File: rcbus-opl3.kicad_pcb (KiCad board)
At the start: 2 copper layers, 100 x 50 mm, 39 parts, among them CON1 SJ1-3523N, P1 RC2014 BUS, U1 74HCT688, U2 YMF262, U3 YAC512, U4 TL074, Y1 SG-8002CA

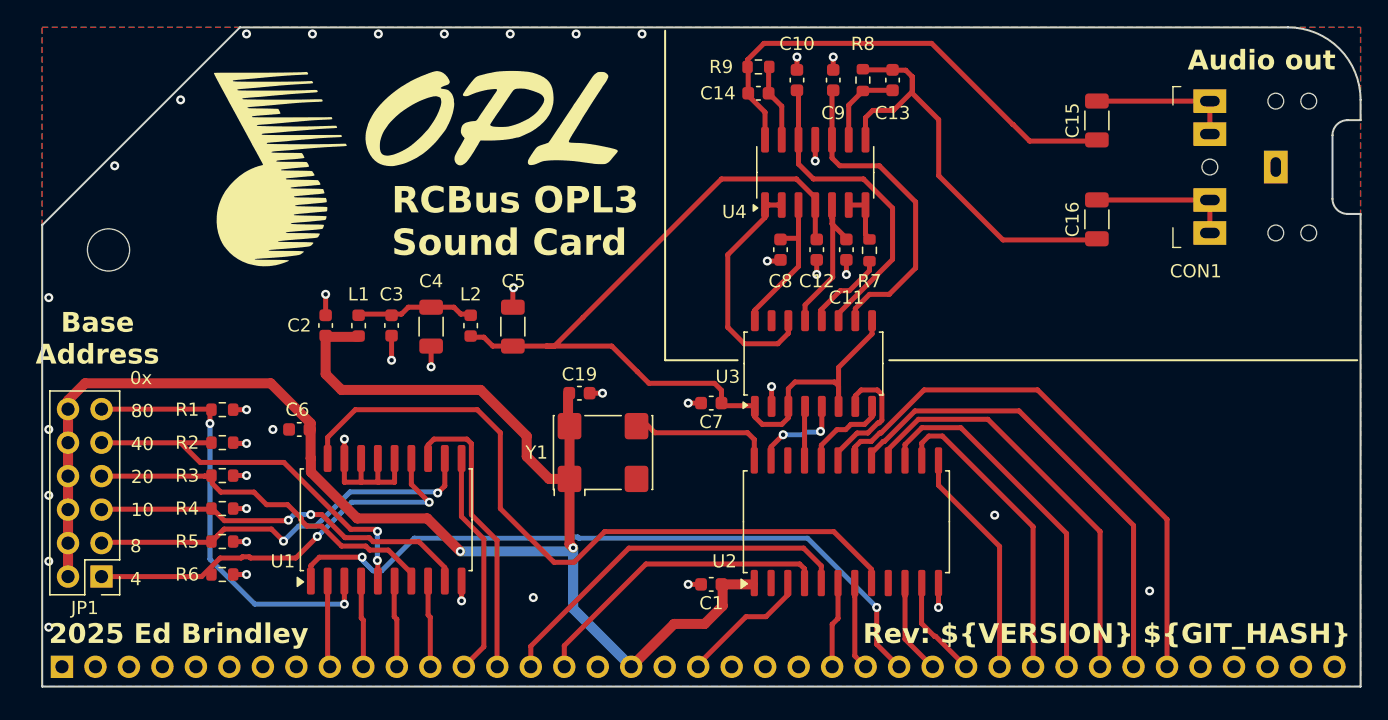
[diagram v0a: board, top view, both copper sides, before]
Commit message: remove unneeded components, some layour rejigging
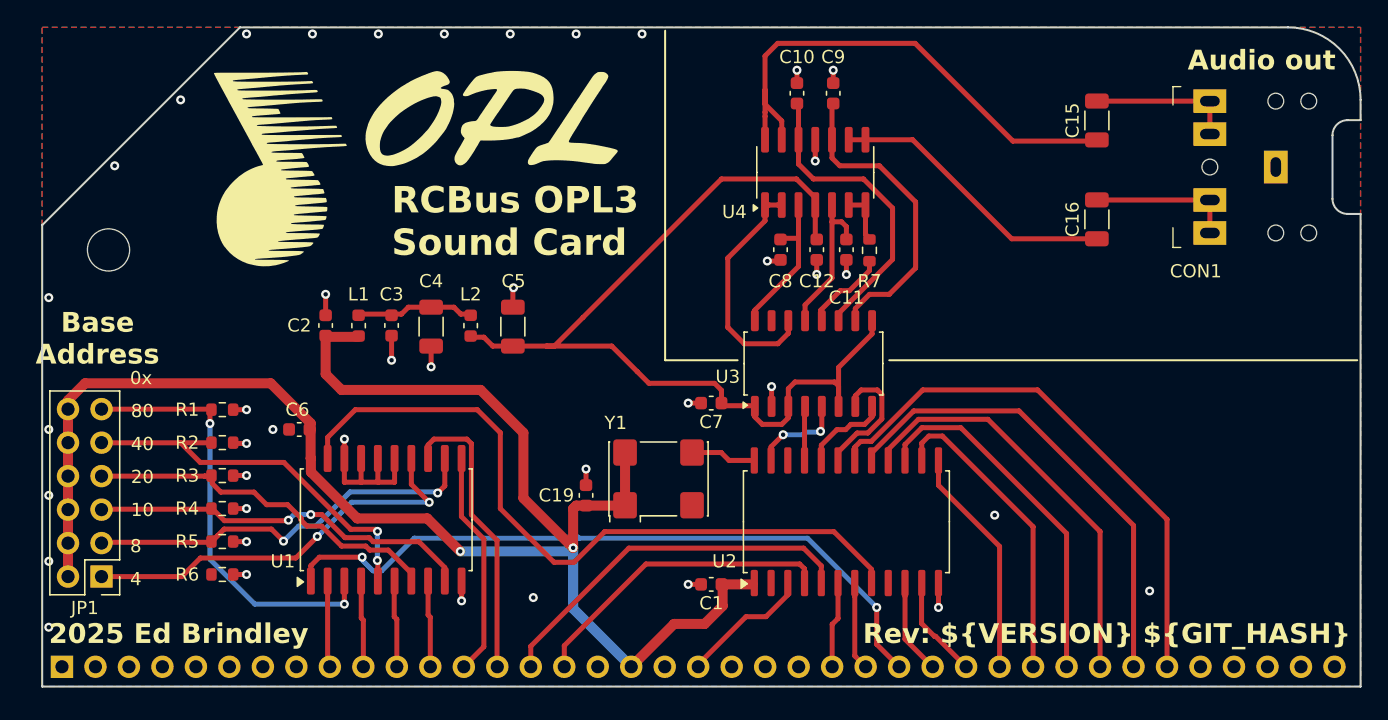
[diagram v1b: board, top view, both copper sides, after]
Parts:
- removed C13, C14: 470pF, Capacitor_SMD:C_0603_1608Metric
- removed R8, R9: 15k, Resistor_SMD:R_0603_1608Metric
- moved C19 7.77 mm to (101.8, 150.0), turned to 90 degrees
- moved Y1 4.66 mm to (107.2, 148.8)
- moved C10 1.00 mm to (117.8, 119.5)
- moved C9 1.00 mm to (120.5, 119.5)
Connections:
- U4 pad 13: Net-(U4D--) -> /L
- U4 pad 9: Net-(U4C--) -> /R
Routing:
- net /R: track 33.3 -> 21.9 mm
- net Net-(U4C--): track 6.34 -> 0.00 mm
- net /CLK: track 10.9 -> 4.97 mm
- net Net-(U4D--): track 5.88 -> 0.00 mm
- net VCC: track 123.3 -> 127.0 mm
- net /L: track 36.6 -> 39.3 mm
- net /AUDIO_CH2: track 23.7 -> 22.8 mm
- net Net-(U3-AOUT): track 12.6 -> 11.8 mm
- net /AUDIO_CH1: track 24.5 -> 23.7 mm

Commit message: add additional output caps/ resistors
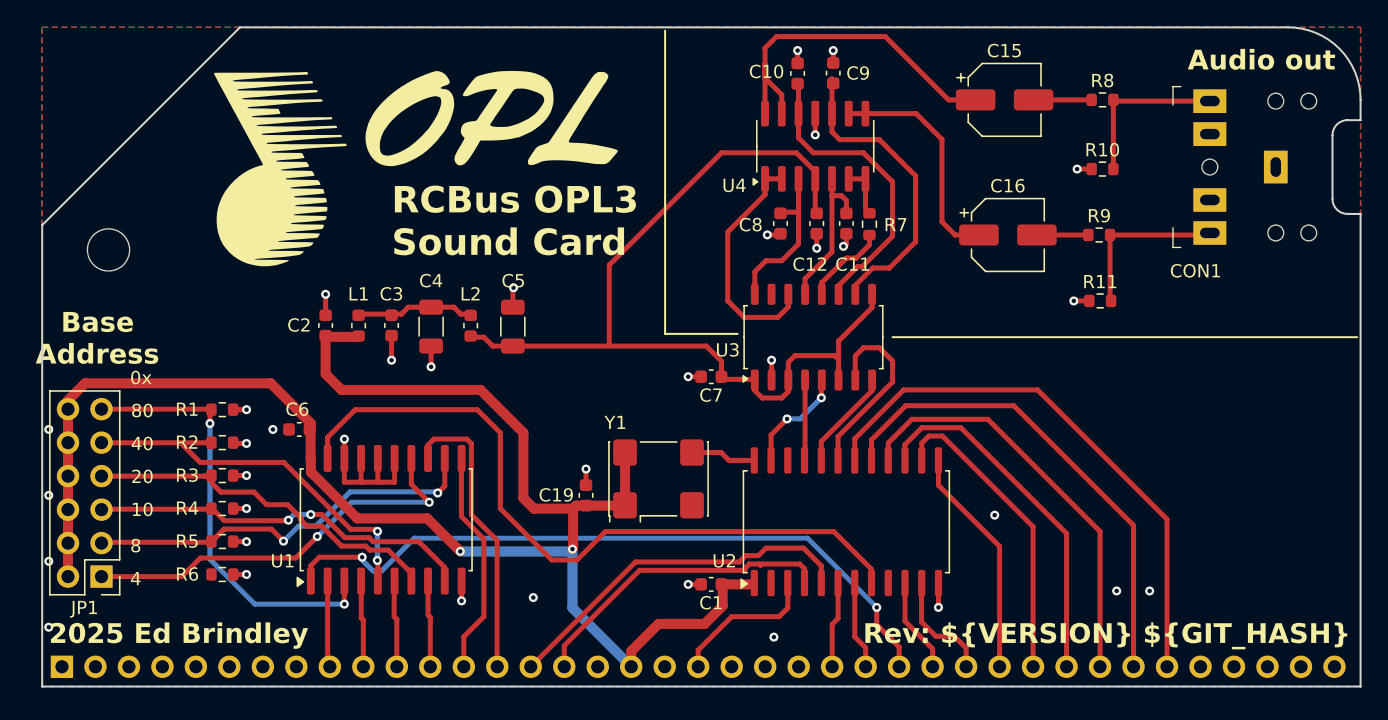
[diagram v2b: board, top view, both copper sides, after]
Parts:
- added R10: 10K, Resistor_SMD:R_0603_1608Metric, F.Cu at (140.9, 125.2)
- added R11: 10K, Resistor_SMD:R_0603_1608Metric, F.Cu at (140.8, 135.2)
- added R8: 100, Resistor_SMD:R_0603_1608Metric, F.Cu at (140.9, 120.0)
- added R9: 100, Resistor_SMD:R_0603_1608Metric, F.Cu at (140.7, 130.2)
- C15, C16: footprint Capacitor_SMD:C_1206_3216Metric -> Capacitor_SMD:CP_Elec_5x5.9
- moved C15 7.17 mm to (133.5, 120.0), turned to 0 degrees
- moved C16 6.85 mm to (133.8, 130.2), turned to 0 degrees
- moved C7 2.00 mm to (111.2, 141.0)
- moved U3 2.00 mm to (119.0, 138.0)
- moved C11 1.98 mm to (121.5, 129.4)
- moved C12 1.98 mm to (119.2, 129.4)
- moved C8 1.98 mm to (116.5, 129.4)
- moved R7 1.98 mm to (123.2, 129.4)
- moved U4 1.98 mm to (119.1, 123.5)
- moved C9 1.53 mm to (120.5, 118.0)
- moved C10 1.50 mm to (117.8, 118.0)
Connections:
- CON1 pad R: Net-(C16-Pad2) -> Net-(CON1-PadR)
- CON1 pad RN: Net-(C16-Pad2) -> Net-(CON1-PadR)
- CON1 pad T: Net-(C15-Pad2) -> Net-(CON1-PadT)
- CON1 pad TN: Net-(C15-Pad2) -> Net-(CON1-PadT)
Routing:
- net Net-(CON1-PadR): track 0.00 -> 12.6 mm
- net Net-(CON1-PadT): track 0.00 -> 12.5 mm
- net /L: track 39.3 -> 27.6 mm
- net Net-(C16-Pad2): track 11.0 -> 3.65 mm
- net Net-(C15-Pad2): track 11.0 -> 4.40 mm
- net /SMPBD: track 9.37 -> 14.6 mm
- net /R: track 21.9 -> 17.3 mm
- net /DOAB: track 4.06 -> 6.06 mm
- net GND: track 37.2 -> 38.9 mm, vias 41 -> 35
- net +5VA: track 71.8 -> 70.5 mm
- net /~{RESET}: track 9.77 -> 11.0 mm
- net /DAC_CLK: track 7.21 -> 8.23 mm
- net /SMPAC: track 6.69 -> 7.69 mm
- net /A1: track 28.5 -> 27.6 mm
- net /D6: track 35.5 -> 36.4 mm
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
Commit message: remove some unusted stuff from kibot, update schematic and pcb
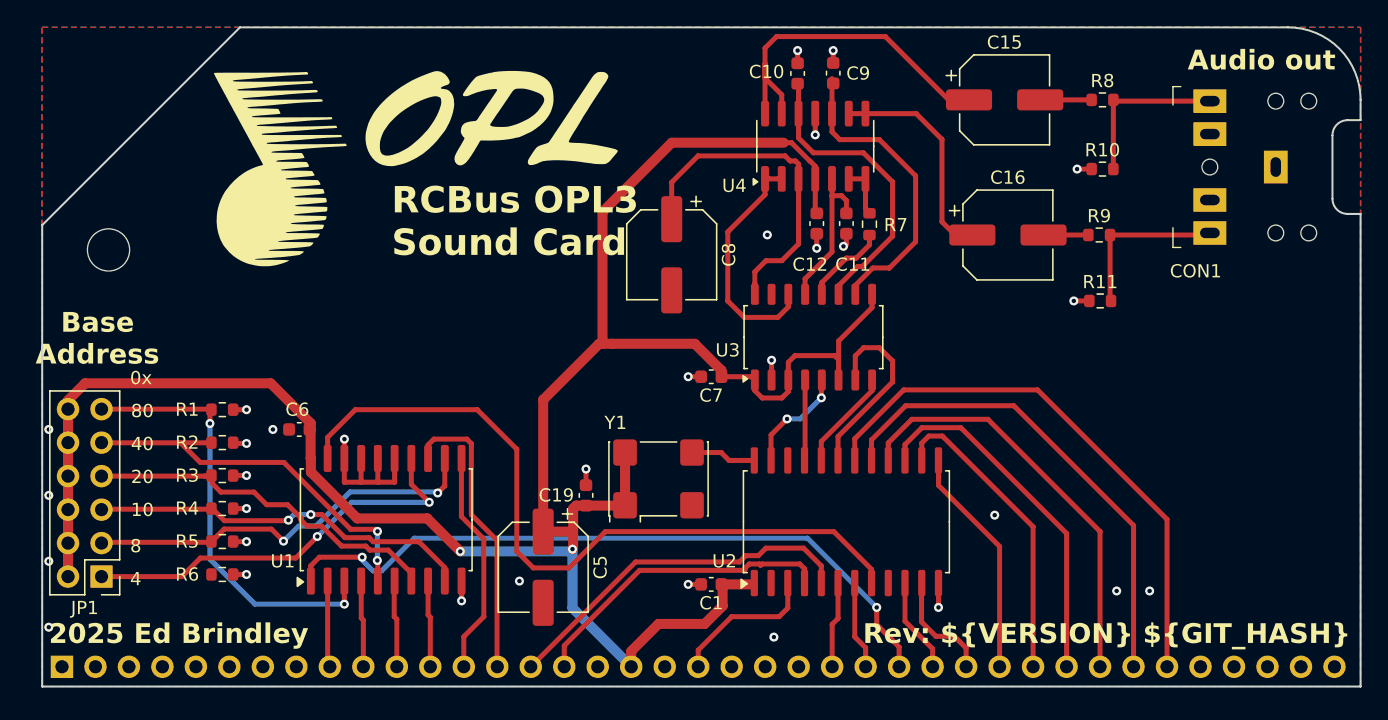
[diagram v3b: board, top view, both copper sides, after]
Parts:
- removed C2: 10nF, Capacitor_SMD:C_0603_1608Metric
- removed C3: 100nF, Capacitor_SMD:C_0603_1608Metric
- removed C4: 10uF, Capacitor_SMD:C_1206_3216Metric
- removed L1: BLM18PG221SN1D, Inductor_SMD:L_0603_1608Metric
- removed L2: 33uH, Inductor_SMD:L_0603_1608Metric
- C15, C16: footprint Capacitor_SMD:CP_Elec_5x5.9 -> Capacitor_SMD:CP_Elec_6.3x5.8
- C5: value 10uF -> 100uF; footprint Capacitor_SMD:C_1206_3216Metric -> Capacitor_SMD:CP_Elec_6.3x7.7
- C8: footprint Capacitor_SMD:C_0603_1608Metric -> Capacitor_SMD:CP_Elec_6.3x5.8
- moved C5 18.4 mm to (98.5, 155.4), turned to -90 degrees
- moved C8 8.58 mm to (108.2, 131.8)
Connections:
- C1 pad 1: VCC -> +5V
- C12 pad 1: +5VA -> +5V
- C19 pad 1: VCC -> +5V
- C5 pad 1: +5VA -> +5V
- C6 pad 1: VCC -> +5V
- C7 pad 1: +5VA -> +5V
- JP1 pad 10: VCC -> +5V
- JP1 pad 12: VCC -> +5V
- JP1 pad 2: VCC -> +5V
- JP1 pad 4: VCC -> +5V
- JP1 pad 6: VCC -> +5V
- JP1 pad 8: VCC -> +5V
- P1 pad 18: VCC -> +5V
- U1 pad 20: VCC -> +5V
- U2 pad 1: VCC -> +5V
- U3 pad 1: +5VA -> +5V
- U3 pad 3: +5VA -> +5V
- U3 pad 6: +5VA -> +5V
- U3 pad 9: +5VA -> +5V
- U4 pad 4: +5VA -> +5V
- Y1 pad 1: VCC -> +5V
- Y1 pad 4: VCC -> +5V
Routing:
- net +5V: track 0.00 -> 178.2 mm, vias 0 -> 2
- net VCC: track 126.4 -> 0.00 mm, vias 2 -> 0
- net +5VA: track 70.5 -> 0.00 mm
- net Net-(U3-CV): track 12.2 -> 25.5 mm
- net Net-(C3-Pad1): track 8.93 -> 0.00 mm
- net GND: track 38.9 -> 31.6 mm, vias 35 -> 31
- net /~{CS}: track 54.9 -> 56.6 mm

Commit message: as submitted for design review on reddit
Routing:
- net GND: vias 31 -> 28
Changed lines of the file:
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@@
 			(psnegative no)
 			(psa4output no)
-			(plot_black_and_white yes)
+			(plot_black_and_white no)
 			(sketchpadsonfab no)
 			(plotpadnumbers no)
@@
 			(crossoutdnponfab yes)
 			(subtractmaskfromsilk no)
-			(outputformat 1)
+			(outputformat 4)
 			(mirror no)
 			(drillshape 0)
@@
 	)
 	(via
-		(at 61 155)
-		(size 0.6858)
-		(drill 0.3302)
-		(layers "F.Cu" "B.Cu")
-		(free yes)
-		(net 2)
-	)
-	(via
 		(at 117.8 116.258122)
 		(size 0.6858)
@@
 	)
 	(via
-		(at 61 150)
-		(size 0.6858)
-		(drill 0.3302)
-		(layers "F.Cu" "B.Cu")
-		(free yes)
-		(net 2)
-	)
-	(via
 		(at 120.5 116.258122)
 		(size 0.6858)
@@
 		(size 0.6858)
 		(drill 0.3302)
-		(layers "F.Cu" "B.Cu")
-		(free yes)
-		(net 2)
-	)
-	(via
-		(at 61 145)
-		(size 0.6858)
-		(drill 0.3302)

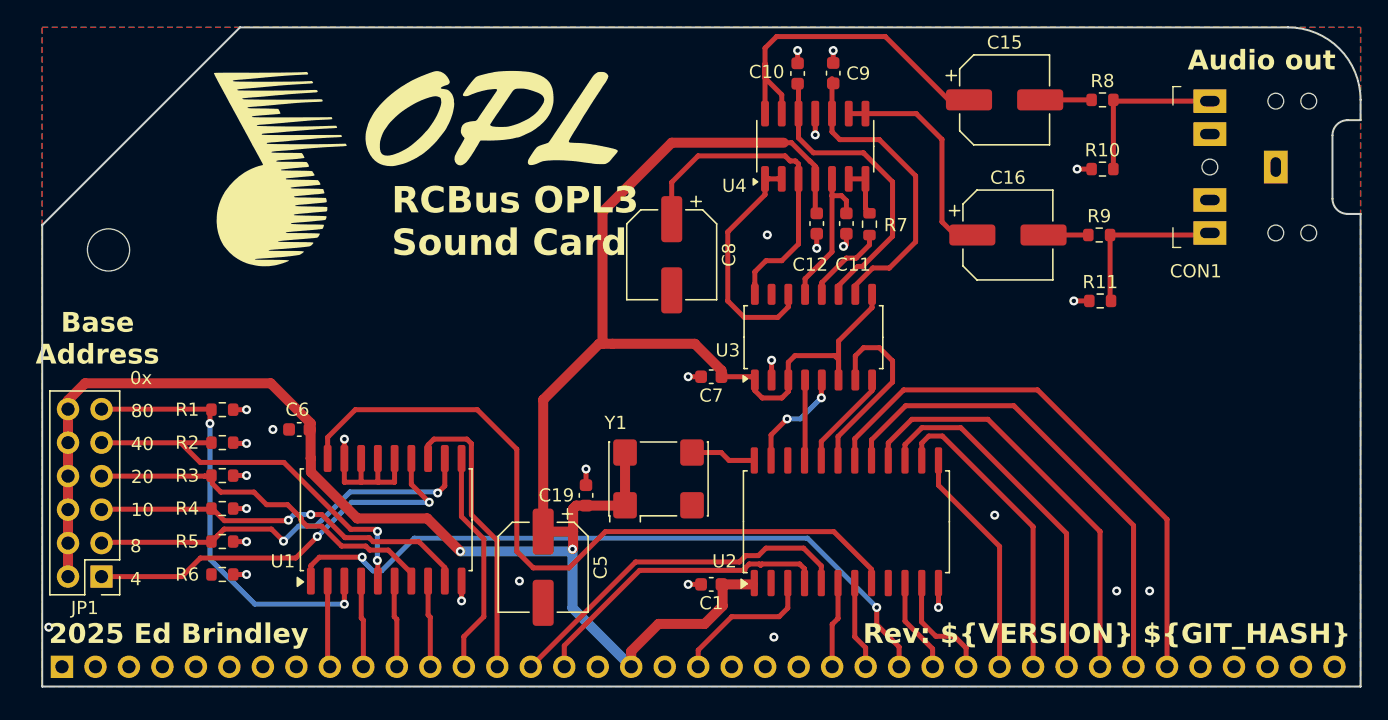
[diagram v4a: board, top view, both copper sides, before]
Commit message: reroute. add additional bulk cap
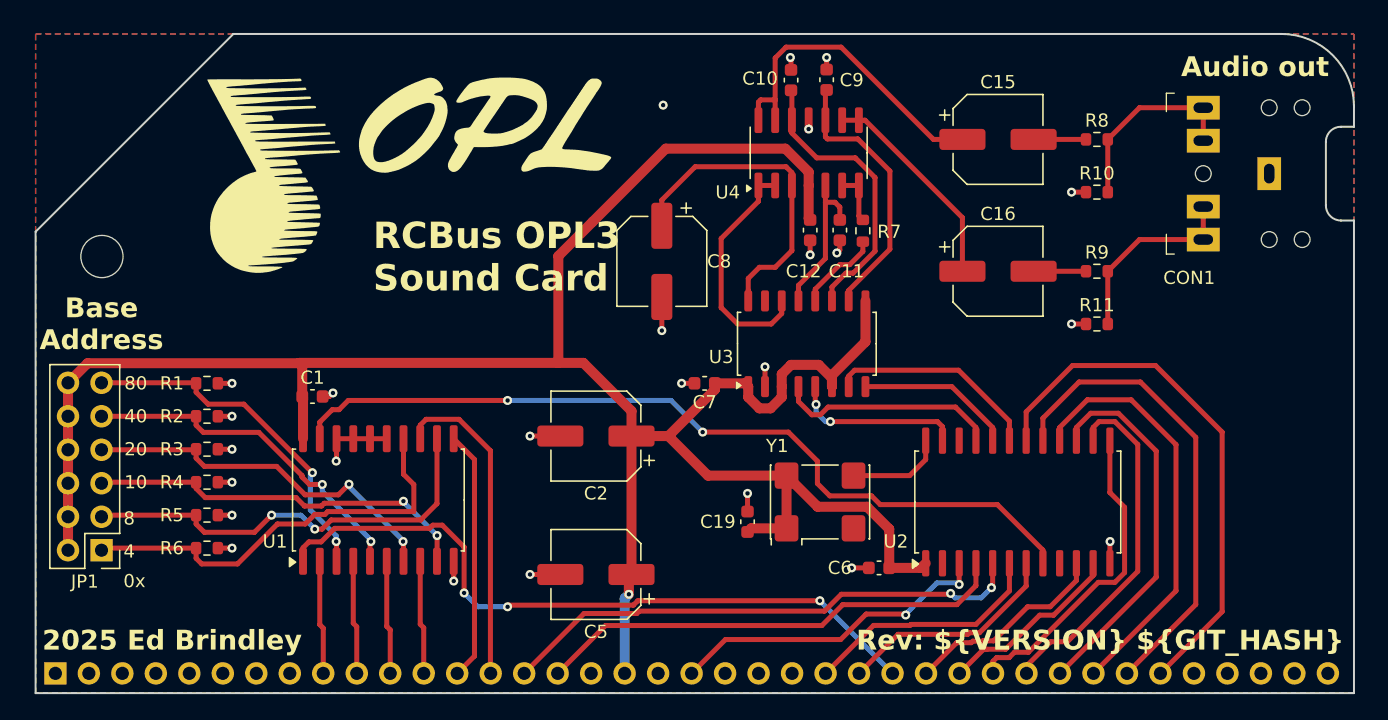
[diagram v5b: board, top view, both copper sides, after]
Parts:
- added C2: 10uf, Capacitor_SMD:CP_Elec_6.3x5.8, F.Cu at (102.5, 145.5)
- CON1: value SJ1-3523N -> 3.5mm jack
- Y1: value SG-8002CA -> 14.3181MHz
- moved C6 45.2 mm to (124.0, 155.5)
- moved C1 33.4 mm to (81.0, 142.5), turned to 0 degrees
- moved U2 13.1 mm to (134.5, 150.5)
- moved C19 12.4 mm to (114.0, 152.0)
- moved Y1 12.4 mm to (119.5, 150.5)
- moved C5 4.04 mm to (102.5, 156.0), turned to 180 degrees
- moved C15 3.04 mm to (133.0, 123.0)
- moved R8 3.03 mm to (140.5, 123.0)
- moved C16 2.85 mm to (133.0, 133.0)
- moved R9 2.76 mm to (140.5, 133.0)
- moved R1 2.31 mm to (73.0, 141.5)
- moved R2 2.31 mm to (73.0, 144.0)
- moved R3 2.31 mm to (73.0, 146.5)
- moved R4 2.31 mm to (73.0, 149.0)
- moved R5 2.31 mm to (73.0, 151.5)
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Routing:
- net /~{RESET}: track 11.0 -> 24.9 mm, vias 0 -> 2
- net /A1: track 27.6 -> 40.3 mm, vias 0 -> 2
- net /A0: track 23.8 -> 36.2 mm
- net /~{WR}: track 6.53 -> 18.6 mm
- net /DOAB: track 6.06 -> 16.9 mm
- net /~{RD}: track 6.69 -> 17.1 mm
- net /D0: track 7.22 -> 15.6 mm
- net /~{CS}: track 56.6 -> 63.5 mm, vias 0 -> 2
- net /D2: track 17.6 -> 24.2 mm
- net Net-(JP1-Pin_11): track 32.7 -> 26.8 mm
- net /D1: track 8.56 -> 14.1 mm
- net /DAC_CLK: track 8.23 -> 13.1 mm
- net /SMPAC: track 7.69 -> 11.9 mm
- net /D3: track 23.5 -> 26.9 mm
- net GND: track 31.6 -> 34.7 mm, vias 28 -> 25
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
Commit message: rotate u2
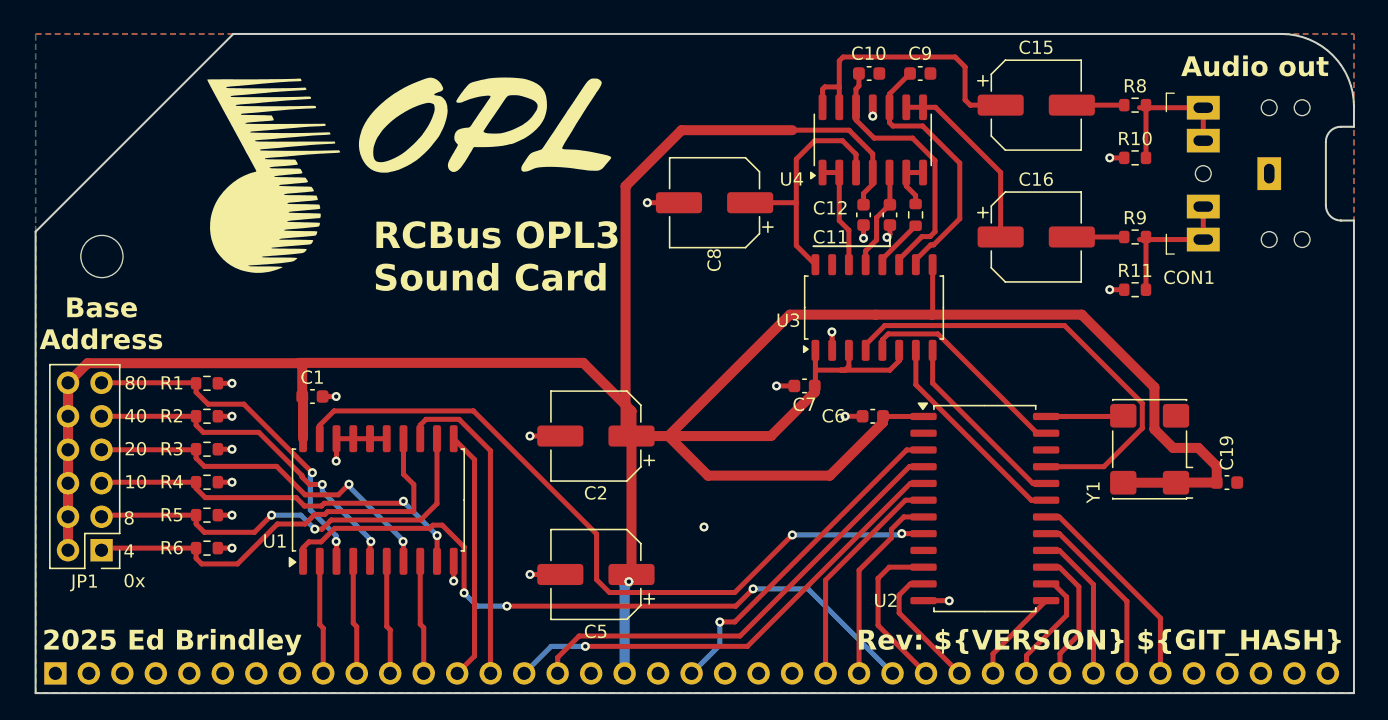
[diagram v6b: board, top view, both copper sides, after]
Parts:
- moved C19 36.5 mm to (150.4, 149.0), turned to 0 degrees
- moved Y1 25.3 mm to (144.5, 146.5), turned to 90 degrees
- moved C6 11.5 mm to (123.5, 144.0)
- moved C7 7.58 mm to (118.3, 141.7)
- moved C9 7.12 mm to (127.1, 118.0), turned to 0 degrees
- moved C8 5.98 mm to (111.5, 127.8), turned to 180 degrees
- moved C10 5.95 mm to (123.2, 118.0), turned to 0 degrees
- moved U3 5.79 mm to (123.6, 135.8)
- moved U4 4.96 mm to (123.5, 123.0)
- moved C12 4.21 mm to (122.8, 128.7)
- moved R7 4.18 mm to (126.8, 128.7)
- moved C11 3.97 mm to (124.8, 128.7)
- moved C15 3.89 mm to (135.9, 120.4)
- moved C16 3.89 mm to (135.9, 130.4)
- moved R10 3.89 mm to (143.4, 124.4)
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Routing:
- net +5V: track 180.4 -> 242.3 mm
- net /D7: track 40.8 -> 16.0 mm
- net /D6: track 36.2 -> 13.7 mm
- net /D5: track 32.0 -> 11.4 mm
- net /D3: track 26.9 -> 8.45 mm
- net /D4: track 28.6 -> 10.3 mm
- net /DOAB: track 16.9 -> 34.4 mm
- net /D2: track 24.2 -> 7.18 mm
- net Net-(U3-MP): track 18.1 -> 8.56 mm
- net /~{CS}: track 63.5 -> 56.8 mm
- net Net-(U3-CV): track 25.1 -> 19.0 mm
- net Net-(U3-AOUT): track 11.8 -> 7.72 mm
- net /D1: track 14.1 -> 10.0 mm
- net /A1: track 40.3 -> 36.3 mm, vias 2 -> 1
- net Net-(CON1-PadT): track 14.7 -> 11.3 mm
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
